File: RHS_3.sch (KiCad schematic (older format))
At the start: 35 parts, among them IC1 ATMEGA328P-A, IC2 CC1101, P4 ISP Bottom, P5 ISP Top, P6 FTDI, P7 ISP 10, SW1 Reset, SW2 Config, U1 TLE4913, U2 TLE4913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

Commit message: v1.1
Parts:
- removed JP1, JP2: SolderJumper_3_Open, Jumper:SolderJumper-3_P1.3mm_Open_Pad1.0x1.5mm_NumberLabels, symbol Jumper:SolderJumper_3_Open
- added C13: 10p, Capacitor_SMD:C_0805_2012Metric_Pad1.15x1.40mm_HandSolder, symbol RHS_3-rescue:C-RHS_2-rescue
- added J1: Glass Breakage Detector, TerminalBlock:TerminalBlock_bornier-2_P5.08mm, symbol Connector:Screw_Terminal_01x02
- added J2: ANT, Connector_Pin:Pin_D1.0mm_L10.0mm, symbol Connector_Generic:Conn_01x01
- added R7: 1M, Resistor_SMD:R_0805_2012Metric_Pad1.15x1.40mm_HandSolder, symbol RHS_3-rescue:R-RHS_2-rescue
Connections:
- wire segments 174 -> 181
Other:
- moved on the sheet: C4, C5, C6, R4, R5, R6, U1, U2, U3

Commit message: V1.1 ready
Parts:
- C1, C2, C3, C7: LCSC Part # (none) -> C49678
- C10, C13, C8, C9: LCSC Part # (none) -> C1785
- C4, C5, C6: LCSC Part # (none) -> C1710
- D1: LCSC Part # (none) -> C84256
- D2: LCSC Part # (none) -> C2297
- IC1: LCSC Part # (none) -> C14877
- J1: footprint TerminalBlock:TerminalBlock_bornier-2_P5.08mm -> Connector_JST:JST_XH_S2B-XH-A-1_1x02_P2.50mm_Horizontal; Reichelt (none) -> https://www.reichelt.de/jst-stiftleiste-gerade-1x2-polig-xh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
- R1: LCSC Part # (none) -> C17414
- R2, R3: LCSC Part # (none) -> C4310
- R4, R5, R6, R7: LCSC Part # (none) -> C17514
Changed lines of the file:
@@
 F 2 "Package_QFP:TQFP-32_7x7mm_P0.8mm" H 4450 3350 50  0001 C CIN
 F 3 "" H 4450 3350 50  0000 C CNN
+F 4 "C14877" H 4450 3350 50  0001 C CNN "LCSC Part #"
 	1    4450 3350
 	1    0    0    -1
@@
 F 2 "Capacitor_SMD:C_0805_2012Metric_Pad1.15x1.40mm_HandSolder" H 2988 2350 50  0001 C CNN
 F 3 "" H 2950 2500 50  0000 C CNN
+F 4 "C49678" H 2950 2500 50  0001 C CNN "LCSC Part #"
 	1    2950 2500
 	1    0    0    -1
@@
 F 2 "Capacitor_SMD:C_0805_2012Metric_Pad1.15x1.40mm_HandSolder" H 3388 2950 50  0001 C CNN
 F 3 "" H 3350 3100 50  0000 C CNN
+F 4 "C49678" H 3350 3100 50  0001 C CNN "LCSC Part #"
 	1    3350 3100
 	1    0    0    -1
@@
 F 2 "Capacitor_SMD:C_0805_2012Metric_Pad1.15x1.40mm_HandSolder" H 6988 2000 50  0001 C CNN
 F 3 "" H 6950 2150 50  0000 C CNN
+F 4 "C49678" H 6950 2150 50  0001 C CNN "LCSC Part #"
 	1    6950 2150
 	1    0    0    -1
@@
 F 2 "LED_SMD:LED_0805_2012Metric_Pad1.15x1.40mm_HandSolder" H 6450 4550 50  0001 C CNN
 F 3 "" H 6450 4550 50  0000 C CNN
+F 4 "C84256" H 6450 4550 50  0001 C CNN "LCSC Part #"
 	1    6450 4550
 	-1   0    0    1
@@
 F 2 "LED_SMD:LED_0805_2012Metric_Pad1.15x1.40mm_HandSolder" H 6450 4950 50  0001 C CNN
 F 3 "" H 6450 4950 50  0000 C CNN
+F 4 "C2297" H 6450 4950 50  0001 C CNN "LCSC Part #"
 	1    6450 4950
 	-1   0    0    1
@@
 F 2 "Resistor_SMD:R_0805_2012Metric_Pad1.15x1.40mm_HandSolder" V 5780 3500 50  0001 C CNN
 F 3 "" H 5850 3500 50  0000 C CNN
+F 4 "C17414" H 5850 3500 50  0001 C CNN "LCSC Part #"
 	1    5850 3500
 	1    0    0    -1
@@
 F 2 "Resistor_SMD:R_0805_2012Metric_Pad1.15x1.40mm_HandSolder" V 5930 4550 50  0001 C CNN
 F 3 "" H 6000 4550 50  0000 C CNN
+F 4 "C4310" H 6000 4550 50  0001 C CNN "LCSC Part #"
 	1    6000 4550
 	0    1    1    0
@@
 F 2 "Resistor_SMD:R_0805_2012Metric_Pad1.15x1.40mm_HandSolder" V 5930 4950 50  0001 C CNN
 F 3 "" H 6000 4950 50  0000 C CNN
+F 4 "C4310" H 6000 4950 50  0001 C CNN "LCSC Part #"
 	1    6000 4950
 	0    1    1    0
@@
 F 2 "Resistor_SMD:R_0805_2012Metric_Pad1.15x1.40mm_HandSolder" V 7730 3950 50  0001 C CNN
 F 3 "" H 7800 3950 50  0000 C CNN
+F 4 "C17514" H 7800 3950 50  0001 C CNN "LCSC Part #"
 	1    7800 3950
 	1    0    0    -1
@@
 F 2 "Resistor_SMD:R_0805_2012Metric_Pad1.15x1.40mm_HandSolder" V 7930 3950 50  0001 C CNN
 F 3 "" H 8000 3950 50  0000 C CNN
+F 4 "C17514" H 8000 3950 50  0001 C CNN "LCSC Part #"
 	1    8000 3950
 	1    0    0    -1
@@
 F 2 "Resistor_SMD:R_0805_2012Metric_Pad1.15x1.40mm_HandSolder" V 8130 3950 50  0001 C CNN
 F 3 "" H 8200 3950 50  0000 C CNN
+F 4 "C17514" H 8200 3950 50  0001 C CNN "LCSC Part #"
 	1    8200 3950
 	1    0    0    -1
@@
 F 2 "Capacitor_SMD:C_0805_2012Metric_Pad1.15x1.40mm_HandSolder" H 8888 5700 50  0001 C CNN
 F 3 "" H 8850 5850 50  0000 C CNN
+F 4 "C1710" H 8850 5850 50  0001 C CNN "LCSC Part #"
 	1    8850 5850
 	1    0    0    -1
@@
 F 2 "Capacitor_SMD:C_0805_2012Metric_Pad1.15x1.40mm_HandSolder" H 9188 5700 50  0001 C CNN
 F 3 "" H 9150 5850 50  0000 C CNN
+F 4 "C1710" H 9150 5850 50  0001 C CNN "LCSC Part #"
 	1    9150 5850
 	1    0    0    -1
@@
 F 2 "Capacitor_SMD:C_0805_2012Metric_Pad1.15x1.40mm_HandSolder" H 9438 5700 50  0001 C CNN
 F 3 "" H 9400 5850 50  0000 C CNN
+F 4 "C1710" H 9400 5850 50  0001 C CNN "LCSC Part #"
 	1    9400 5850
 	1    0    0    -1
@@
 F 2 "Capacitor_SMD:C_0805_2012Metric_Pad1.15x1.40mm_HandSolder" H 2088 5000 50  0001 C CNN
 F 3 "" H 2050 5150 50  0000 C CNN
+F 4 "C49678" H 2050 5150 50  0001 C CNN "LCSC Part #"
 	1    2050 5150
 	0    1    1    0
@@
 F 2 "Capacitor_SMD:C_0805_2012Metric_Pad1.15x1.40mm_HandSolder" H 8238 5700 50  0001 C CNN
 F 3 "" H 8200 5850 50  0000 C CNN
+F 4 "C1785" H 8200 5850 50  0001 C CNN "LCSC Part #"
 	1    8200 5850
 	1    0    0    -1
@@
 F 2 "Capacitor_SMD:C_0805_2012Metric_Pad1.15x1.40mm_HandSolder" H 8038 5700 50  0001 C CNN
 F 3 "" H 8000 5850 50  0000 C CNN
+F 4 "C1785" H 8000 5850 50  0001 C CNN "LCSC Part #"
 	1    8000 5850
 	1    0    0    -1
@@
 F 2 "Capacitor_SMD:C_0805_2012Metric_Pad1.15x1.40mm_HandSolder" H 7838 5700 50  0001 C CNN
 F 3 "" H 7800 5850 50  0000 C CNN
+F 4 "C1785" H 7800 5850 50  0001 C CNN "LCSC Part #"
 	1    7800 5850
 	1    0    0    -1
@@
 F 1 "9p" V 1562 3500 50  0000 C CNN
 F 2 "Capacitor_SMD:C_0805_2012Metric_Pad1.15x1.40mm_HandSolder" H 1700 3500 50  0001 C CNN
-F 3 "~" H 1700 3500 50  0001 C CNN
+F 3 "" H 1700 3500 50  0001 C CNN
 	1    1700 3500
 	0    1    1    0
@@
 F 1 "9p" V 1562 3900 50  0000 C CNN
 F 2 "Capacitor_SMD:C_0805_2012Metric_Pad1.15x1.40mm_HandSolder" H 1700 3900 50  0001 C CNN
-F 3 "~" H 1700 3900 50  0001 C CNN
+F 3 "" H 1700 3900 50  0001 C CNN
 	1    1700 3900
 	0    1    1    0
@@
 F 2 "Resistor_SMD:R_0805_2012Metric_Pad1.15x1.40mm_HandSolder" V 8330 3950 50  0001 C CNN
 F 3 "" H 8400 3950 50  0000 C CNN
+F 4 "C17514" H 8400 3950 50  0001 C CNN "LCSC Part #"
 	1    8400 3950
 	1    0    0    -1
@@
 F 2 "Capacitor_SMD:C_0805_2012Metric_Pad1.15x1.40mm_HandSolder" H 8438 5700 50  0001 C CNN
 F 3 "" H 8400 5850 50  0000 C CNN
+F 4 "C1785" H 8400 5850 50  0001 C CNN "LCSC Part #"
 	1    8400 5850
 	1    0    0    -1
@@
 F 0 "J1" H 9980 5492 50  0000 L CNN
 F 1 "Glass Breakage Detector" H 9980 5401 50  0000 L CNN
-F 2 "TerminalBlock:TerminalBlock_bornier-2_P5.08mm" H 9900 5500 50  0001 C CNN
-F 3 "~" H 9900 5500 50  0001 C CNN
+F 2 "Connector_JST:JST_XH_S2B-XH-A-1_1x02_P2.50mm_Horizontal" H 9900 5500 50  0001 C CNN
+F 3 "https://cdn-reichelt.de/documents/datenblatt/C100/JST_XH_DB_EN.pdf" H 9900 5500 50  0001 C CNN
+F 4 "https://www.reichelt.de/jst-stiftleiste-gerade-1x2-polig-xh-jst-xh2p-st-p185073.html?&trstct=pol_1&nbc=1" H 9900 5500 50  0001 C CNN "Reichelt"
 	1    9900 5500
 	1    0    0    -1

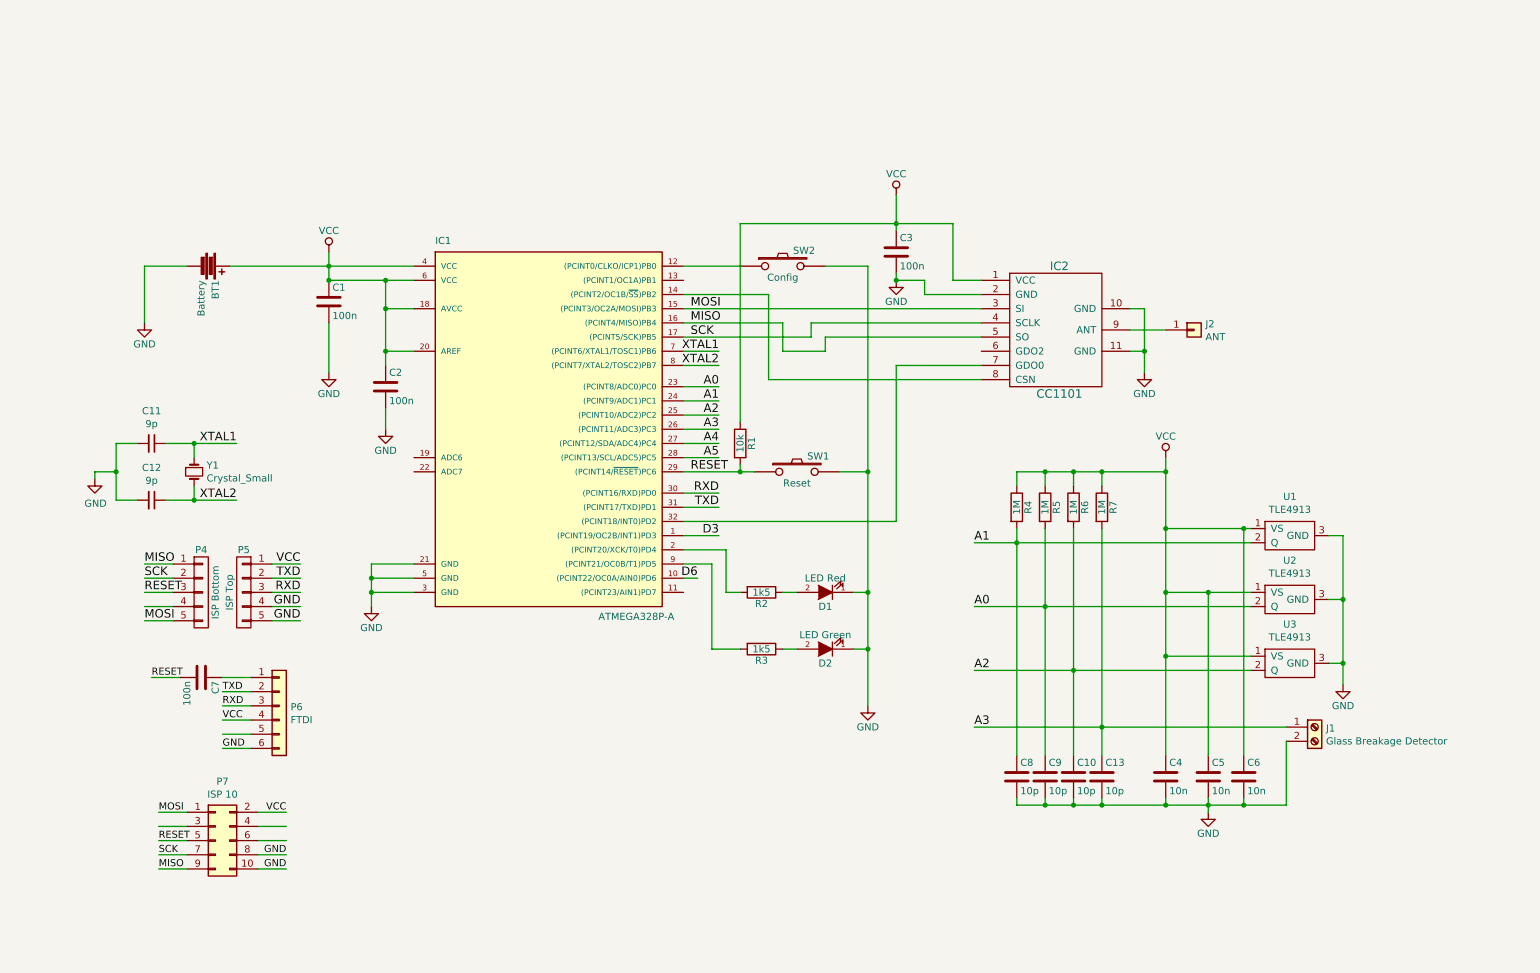
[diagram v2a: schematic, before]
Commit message: optional CC1101 direct use
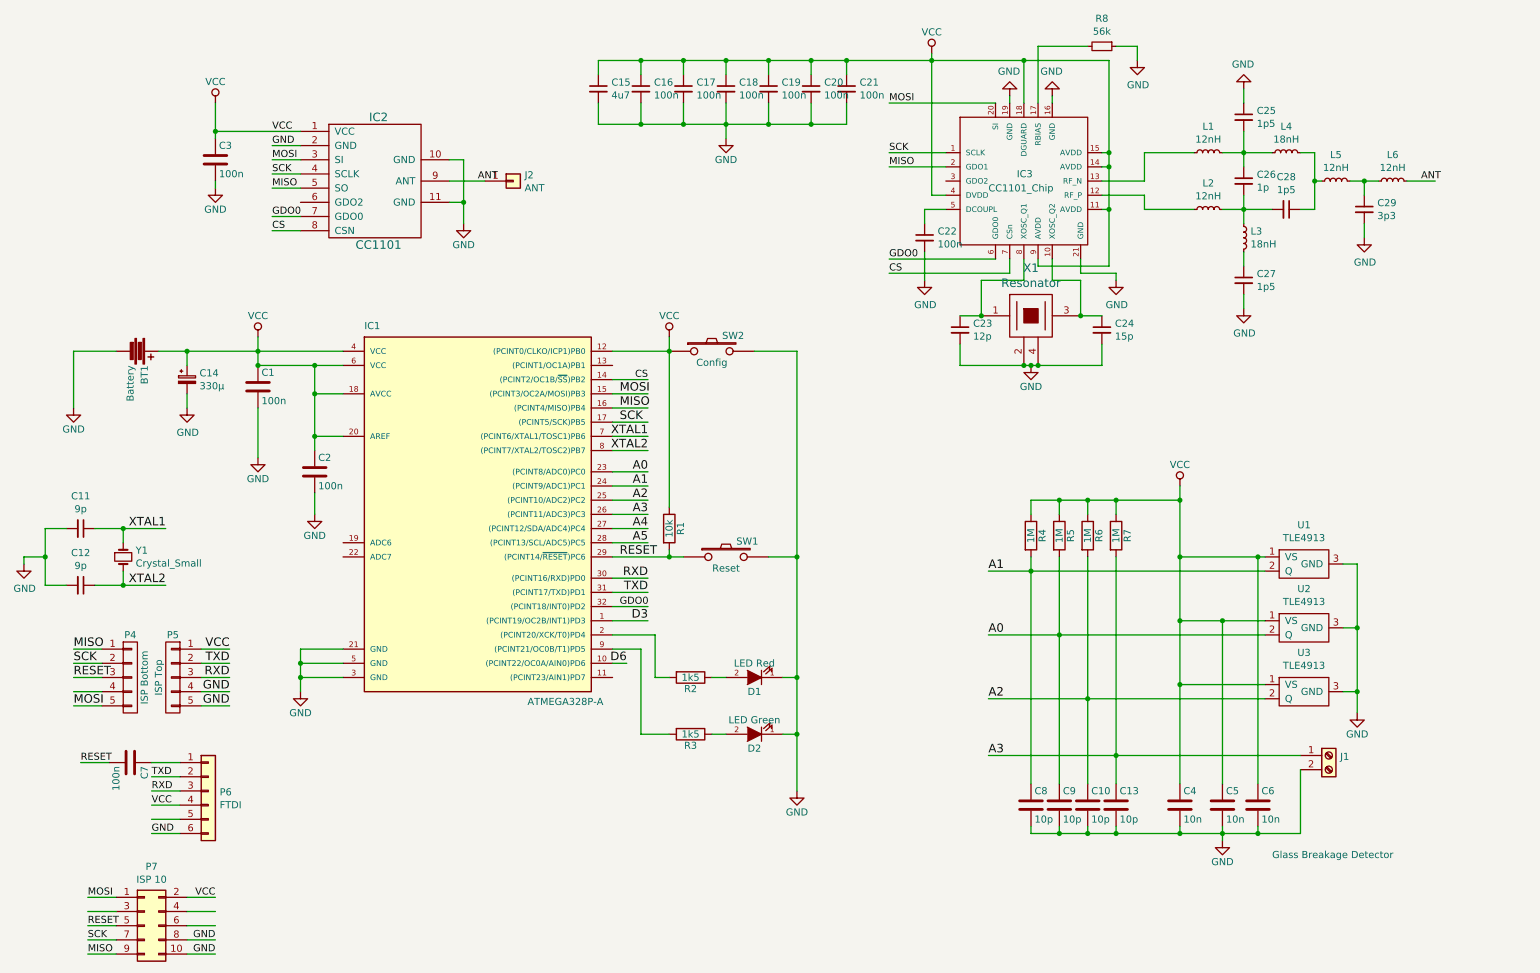
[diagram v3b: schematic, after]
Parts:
- added C14: 330µ, Capacitor_SMD:CP_Elec_6.3x5.8, symbol Device:CP_Small
- added C15: 4u7, Capacitor_SMD:C_0402_1005Metric, symbol Device:C_Small
- added C16, C17, C18, C19, C20, C21, C22: 100n, Capacitor_SMD:C_0402_1005Metric, symbol Device:C_Small
- added C23: 12p, Capacitor_SMD:C_0402_1005Metric, symbol Device:C_Small
- added C24: 15p, Capacitor_SMD:C_0402_1005Metric, symbol Device:C_Small
- added C25, C27, C28: 1p5, Capacitor_SMD:C_0402_1005Metric, symbol Device:C_Small
- added C26: 1p, Capacitor_SMD:C_0402_1005Metric, symbol Device:C_Small
- added C29: 3p3, Capacitor_SMD:C_0402_1005Metric, symbol Device:C_Small
- added IC3: CC1101_Chip, Package_DFN_QFN:QFN-20-1EP_5x5mm_P0.65mm_EP3.35x3.35mm, symbol cc1101:CC1101_Chip
- added L1, L2, L5, L6: 12nH, Inductor_SMD:L_0402_1005Metric, symbol Device:L_Small
- added L3, L4: 18nH, Inductor_SMD:L_0402_1005Metric, symbol Device:L_Small
- added R8: 56k, Resistor_SMD:R_0402_1005Metric, symbol Device:R_Small
- added X1: Resonator, Oscillator:Oscillator_SMD_EuroQuartz_XO32-4Pin_3.2x2.5mm, symbol cc1101:Resonator
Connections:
- net labels added: ANT, CS, GDO0
- wire segments 181 -> 277
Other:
- moved on the sheet: BT1, C1, C10, C11, C12, C13, C2, C3, C4, C5, C6, C7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

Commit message: Jumper added to prepare switch of VCC for CC1101 und Sensors
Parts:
- added JP1, JP2: Jumper_NO_Small, Jumper:SolderJumper-2_P1.3mm_Open_Pad1.0x1.5mm, symbol Device:Jumper_NO_Small
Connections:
- net labels added: VDD, VSS
- wire segments 277 -> 285
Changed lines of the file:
@@
 Title "RHS 3 - CR2477"
 Date ""
-Rev "1.1"
+Rev "2.0"
 Comp ""
 Comment1 ""
@@
 F 3 "" H 2150 1700 50  0000 C CNN
 	1    2150 1700
-	1    0    0    -1
-$EndComp
-$Comp
-L RHS_3-rescue:VCC-RHS_2-rescue #PWR06
-U 1 1 5910649D
-P 2150 1100
-F 0 "#PWR06" H 2150 950 50  0001 C CNN
-F 1 "VCC" H 2150 1250 50  0000 C CNN
-F 2 "" H 2150 1100 50  0000 C CNN
-F 3 "" H 2150 1100 50  0000 C CNN
-	1    2150 1100
 	1    0    0    -1
 $EndComp
@@
 $EndComp
 $Comp
-L RHS_3-rescue:VCC-RHS_2-rescue #PWR0101
-U 1 1 5E6A4AE7
-P 8950 3800
-F 0 "#PWR0101" H 8950 3650 50  0001 C CNN
-F 1 "VCC" H 8950 3950 50  0000 C CNN
-F 2 "" H 8950 3800 50  0000 C CNN
-F 3 "" H 8950 3800 50  0000 C CNN
-	1    8950 3800
-	1    0    0    -1
-$EndComp
-$Comp
 L RHS_3-rescue:R-RHS_2-rescue R4
 U 1 1 5E6B2724
@@
 Wire Wire Line
 	1750 2850 1950 2850
-Wire Wire Line
-	8950 3800 8950 3900
 Wire Wire Line
 	8950 5200 9550 5200
@@
 Text Label 2550 1400 0    50   ~ 0
 GND
-Text Label 2550 1300 0    50   ~ 0
-VCC
 Wire Wire Line
 	4950 3350 5200 3350
@@
 	7200 1750 7300 1750
 Connection ~ 7850 800
-$Comp
-L RHS_3-rescue:VCC-RHS_2-rescue #PWR0110
-U 1 1 5F9DD3AE
-P 7200 750
-F 0 "#PWR0110" H 7200 600 50  0001 C CNN
-F 1 "VCC" H 7200 900 50  0000 C CNN
-F 2 "" H 7200 750 50  0000 C CNN
-F 3 "" H 7200 750 50  0000 C CNN
-	1    7200 750
-	1    0    0    -1
-$EndComp
-Wire Wire Line
-	7200 750  7200 800
 Connection ~ 7200 800
 $Comp
@@
 Wire Wire Line
 	5150 800  5450 800
+$Comp
+L power:VSS #PWR0110
+U 1 1 5F820753
+P 7200 700
+F 0 "#PWR0110" H 7200 550 50  0001 C CNN
+F 1 "VSS" H 7215 873 50  0000 C CNN
+F 2 "" H 7200 700 50  0001 C CNN
+F 3 "" H 7200 700 50  0001 C CNN
+	1    7200 700
+	1    0    0    -1
+$EndComp
+Wire Wire Line
+	7200 700  7200 800
+$Comp
+L power:VSS #PWR0117
+U 1 1 5F83527D
+P 2150 1100
+F 0 "#PWR0117" H 2150 950 50  0001 C CNN
+F 1 "VSS" H 2165 1273 50  0000 C CNN
+F 2 "" H 2150 1100 50  0001 C CNN
+F 3 "" H 2150 1100 50  0001 C CNN
+	1    2150 1100
+	1    0    0    -1
+$EndComp
+$Comp
+L power:VSS #PWR0118
+U 1 1 5F8358EE
+P 7400 3400
+F 0 "#PWR0118" H 7400 3250 50  0001 C CNN
+F 1 "VSS" H 7415 3573 50  0000 C CNN
+F 2 "" H 7400 3400 50  0001 C CNN
+F 3 "" H 7400 3400 50  0001 C CNN
+	1    7400 3400
+	1    0    0    -1
+$EndComp
+$Comp
+L RHS_3-rescue:VCC-RHS_2-rescue #PWR0119
+U 1 1 5F83706C
+P 6750 3400
+F 0 "#PWR0119" H 6750 3250 50  0001 C CNN
+F 1 "VCC" H 6750 3550 50  0000 C CNN
+F 2 "" H 6750 3400 50  0000 C CNN
+F 3 "" H 6750 3400 50  0000 C CNN
+	1    6750 3400
+	1    0    0    -1
+$EndComp
+Text Label 2550 1300 0    50   ~ 0
+VSS
+$Comp
+L power:VDD #PWR0101
+U 1 1 5F87E9D0
+P 8950 3400
+F 0 "#PWR0101" H 8950 3250 50  0001 C CNN
+F 1 "VDD" H 8965 3573 50  0000 C CNN
+F 2 "" H 8950 3400 50  0001 C CNN
+F 3 "" H 8950 3400 50  0001 C CNN
+	1    8950 3400
+	1    0    0    -1
+$EndComp
+$Comp
+L Device:Jumper_NO_Small JP1
+U 1 1 5F8BD3FD
+P 7050 3500
+F 0 "JP1" H 7050 3685 50  0000 C CNN
+F 1 "Jumper_NO_Small" H 7050 3594 50  0000 C CNN
+F 2 "Jumper:SolderJumper-2_P1.3mm_Open_Pad1.0x1.5mm" H 7050 3500 50  0001 C CNN
+F 3 "~" H 7050 3500 50  0001 C CNN
+	1    7050 3500
+	1    0    0    -1
+$EndComp
+$Comp
+L Device:Jumper_NO_Small JP2
+U 1 1 5F8BE151
+P 8650 3500
+F 0 "JP2" H 8650 3685 50  0000 C CNN
+F 1 "Jumper_NO_Small" H 8650 3594 50  0000 C CNN
+F 2 "Jumper:SolderJumper-2_P1.3mm_Open_Pad1.0x1.5mm" H 8650 3500 50  0001 C CNN
+F 3 "~" H 8650 3500 50  0001 C CNN
+	1    8650 3500
+	1    0    0    -1
+$EndComp
+$Comp
+L RHS_3-rescue:VCC-RHS_2-rescue #PWR0120
+U 1 1 5F8E9612
+P 8350 3400
+F 0 "#PWR0120" H 8350 3250 50  0001 C CNN
+F 1 "VCC" H 8350 3550 50  0000 C CNN
+F 2 "" H 8350 3400 50  0000 C CNN
+F 3 "" H 8350 3400 50  0000 C CNN
+	1    8350 3400
+	1    0    0    -1
+$EndComp
+Wire Wire Line
+	8950 3400 8950 3500
+Wire Wire Line
+	8350 3400 8350 3500
+Wire Wire Line
+	8350 3500 8550 3500
+Wire Wire Line
+	8750 3500 8950 3500
+Connection ~ 8950 3500
+Wire Wire Line
+	8950 3500 8950 3900
+Wire Wire Line
+	6750 3400 6750 3500
+Wire Wire Line
+	6750 3500 6950 3500
+Wire Wire Line
+	7150 3500 7400 3500
+Wire Wire Line
+	7400 3500 7400 3400
 $EndSCHEMATC

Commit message: CC1101 footprint fixed
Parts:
- IC3: footprint Package_DFN_QFN:QFN-20-1EP_5x5mm_P0.65mm_EP3.35x3.35mm -> Package_DFN_QFN:QFN-20-1EP_4x4mm_P0.5mm_EP2.5x2.5mm
- JP1, JP2: footprint Jumper:SolderJumper-2_P1.3mm_Open_Pad1.0x1.5mm -> Jumper:SolderJumper-2_P1.3mm_Bridged_Pad1.0x1.5mm
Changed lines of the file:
@@
 F 0 "IC3" H 7800 1700 50  0000 L CNN
 F 1 "CC1101_Chip" H 7600 1600 50  0000 L CNN
-F 2 "Package_DFN_QFN:QFN-20-1EP_5x5mm_P0.65mm_EP3.35x3.35mm" H 7850 1650 50  0001 C CNN
+F 2 "Package_DFN_QFN:QFN-20-1EP_4x4mm_P0.5mm_EP2.5x2.5mm" H 7850 1650 50  0001 C CNN
 F 3 "" H 7850 1650 50  0001 C CNN
 	1    7850 1650
@@
 F 0 "JP1" H 7050 3685 50  0000 C CNN
 F 1 "Jumper_NO_Small" H 7050 3594 50  0000 C CNN
-F 2 "Jumper:SolderJumper-2_P1.3mm_Open_Pad1.0x1.5mm" H 7050 3500 50  0001 C CNN
+F 2 "Jumper:SolderJumper-2_P1.3mm_Bridged_Pad1.0x1.5mm" H 7050 3500 50  0001 C CNN
 F 3 "~" H 7050 3500 50  0001 C CNN
 	1    7050 3500
@@
 F 0 "JP2" H 8650 3685 50  0000 C CNN
 F 1 "Jumper_NO_Small" H 8650 3594 50  0000 C CNN
-F 2 "Jumper:SolderJumper-2_P1.3mm_Open_Pad1.0x1.5mm" H 8650 3500 50  0001 C CNN
+F 2 "Jumper:SolderJumper-2_P1.3mm_Bridged_Pad1.0x1.5mm" H 8650 3500 50  0001 C CNN
 F 3 "~" H 8650 3500 50  0001 C CNN
 	1    8650 3500
